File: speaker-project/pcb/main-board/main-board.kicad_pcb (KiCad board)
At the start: 4 copper layers, 100 x 80 mm, 172 parts, among them J1 XT30U-M, J10 UART0, J11 USB-C, J12 JTAG, J13 BT-Modul, J14 Button-PCB, J2 JST-XH-5, J3 JST-XH-5, J4 CHG-STAT, J5 ICP5/USBi, J6 AuxIn 3.5mm, J7 FR-L, J8 FR-R, J9 SUB, Q1 AO4407A, Q2 AO4407A, Q3 MMBT3904, Q4 BC807-40, SW1 RESET, SW2 BOOT, U1 LMR33630ADDA, U2 AMS1117-3.3, U3 ADAU1701JSTZ, U4 24LC32A, U6 TPA3118D2DAP, U7 TPA3118D2DAP, U8 ESP32-S3-WROOM-1-N8R2, U9 USBLC6-2SC6, Y1 12.288MHz

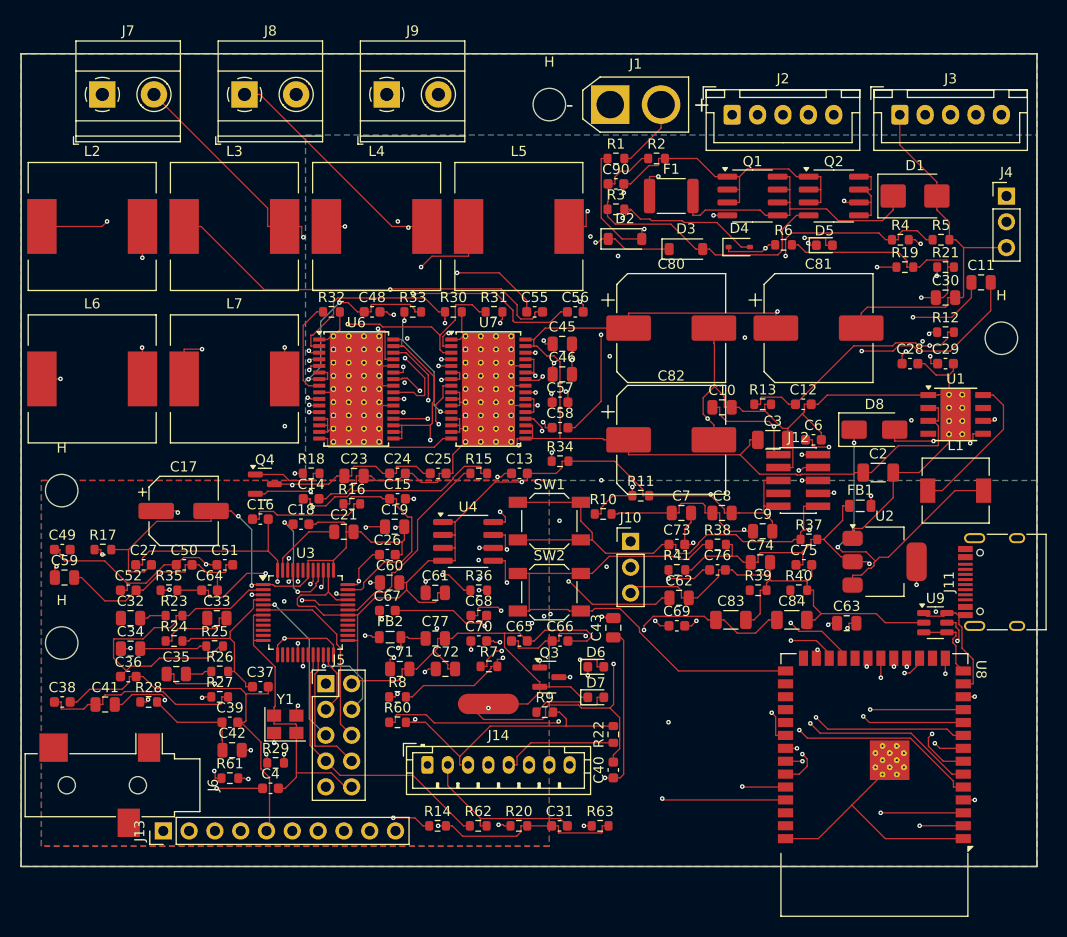
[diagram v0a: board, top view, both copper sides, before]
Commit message: BEIDE PCBs FERTIG GEROUTET: 0 offene Verbindungen, 0 elektrische DRC-Fehler — bestellbar
Main-Board (4-Lagen, via Freerouting vollstaendig verdrahtet, ~2820
Bahnen/Vias): Die letzten Blocker waren Exporter-Bugs, alle behoben:
- Pad-Geometrie rotationsbewusst (GetSize() ignoriert Rotation -> USB-C-
  Pads um 90 Grad falsch, daher alle bisherigen Kollisionen/offene Netze)
- quadratische Pads als Rect statt Kreis (Ecken von J5/J9/EPAD)
- NPTH-Montageloecher als netzlose Hindernisse, eindeutige Referenzen
  (vorher sah Freerouting nur 1 von 4 Loechern 'H')
- Keepouts exportiert: Taster-Hebel SW1/SW2, ESP-Antenne, NT1-Netztie-
  Polygon (Mitte gesperrt, Pad-Zugaenge frei)
- gebohrte Pads +0.56mm aufgeblasen (KiCad-Hole-Clearance 0.25 erfuellt)
- SES-Import: Bahnbreite um->nm, Design-Regeln + Netzklasse (kicad_pro!)
  robust gesetzt, WIRED=1-Modus zum Lueckenschliessen (GVDD1-Inselsplit)
- R10/C5-Platzierung bereinigt (C5=Bootstrap an U1), No-Pour ueber NT1

DRC final: Main 0 unconnected/0 elektrisch, Button 0/0. Fab-Exporte
(4-Lagen-Gerber, BOM, Positions) neu. Docs auf Endstand.

Co-Authored-By: Claude Fable 5 <noreply@anthropic.com>
Claude-Session: https://claude.ai/code/session_01L8xsupY9ovG6C5NDPPgqaH
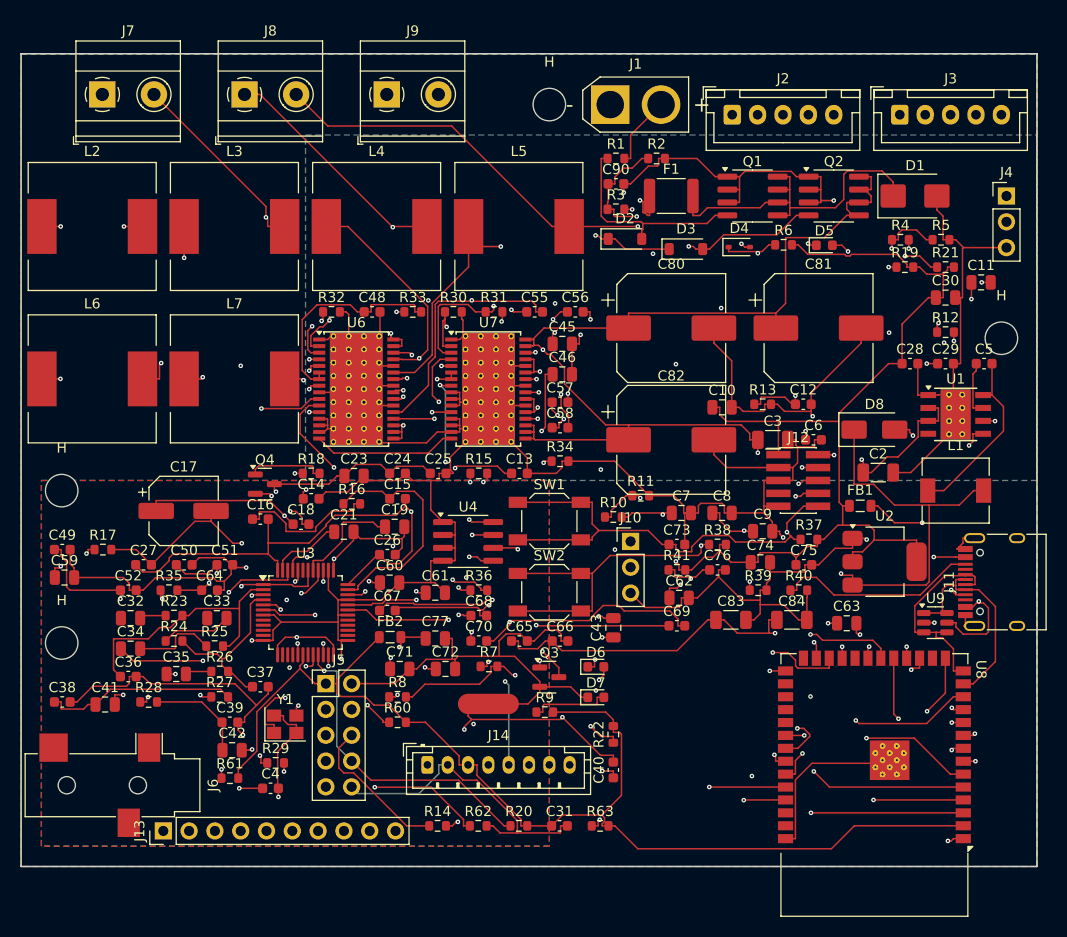
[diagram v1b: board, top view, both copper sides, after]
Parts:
- added C5: 100n, C_0603_1608Metric, F.Cu at (94.8, 30.5)
- moved R10 1.04 mm to (58.3, 45.6)
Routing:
- net 3V3: track 345.5 -> 314.9 mm, vias 16 -> 6
- net CC1: track 0.00 -> 22.6 mm, vias 0 -> 2
- net SUB_OUT_P: track 103.3 -> 124.7 mm, vias 5 -> 3
- net CC2: track 0.00 -> 20.1 mm
- net SDA: track 133.5 -> 150.6 mm, vias 6 -> 4
- net U6_BSPR: track 20.3 -> 36.9 mm
- net U6_BSNR: track 17.7 -> 34.1 mm
- net VBAT_P: track 141.4 -> 126.1 mm, vias 4 -> 5
- net SCL: track 112.6 -> 98.9 mm, vias 2 -> 5
- net USB_DP: track 7.51 -> 20.6 mm
- net U6_RINN: track 31.4 -> 43.7 mm, vias 4 -> 2
- net PVDD: track 281.2 -> 293.3 mm, vias 9 -> 10
- net AMPIN_SUB: track 39.0 -> 49.7 mm
- net SUB_OUT_N: track 89.1 -> 78.7 mm
- net USB_DN: track 12.1 -> 22.1 mm
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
